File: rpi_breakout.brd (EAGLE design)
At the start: 33 x 54 mm, 21 parts

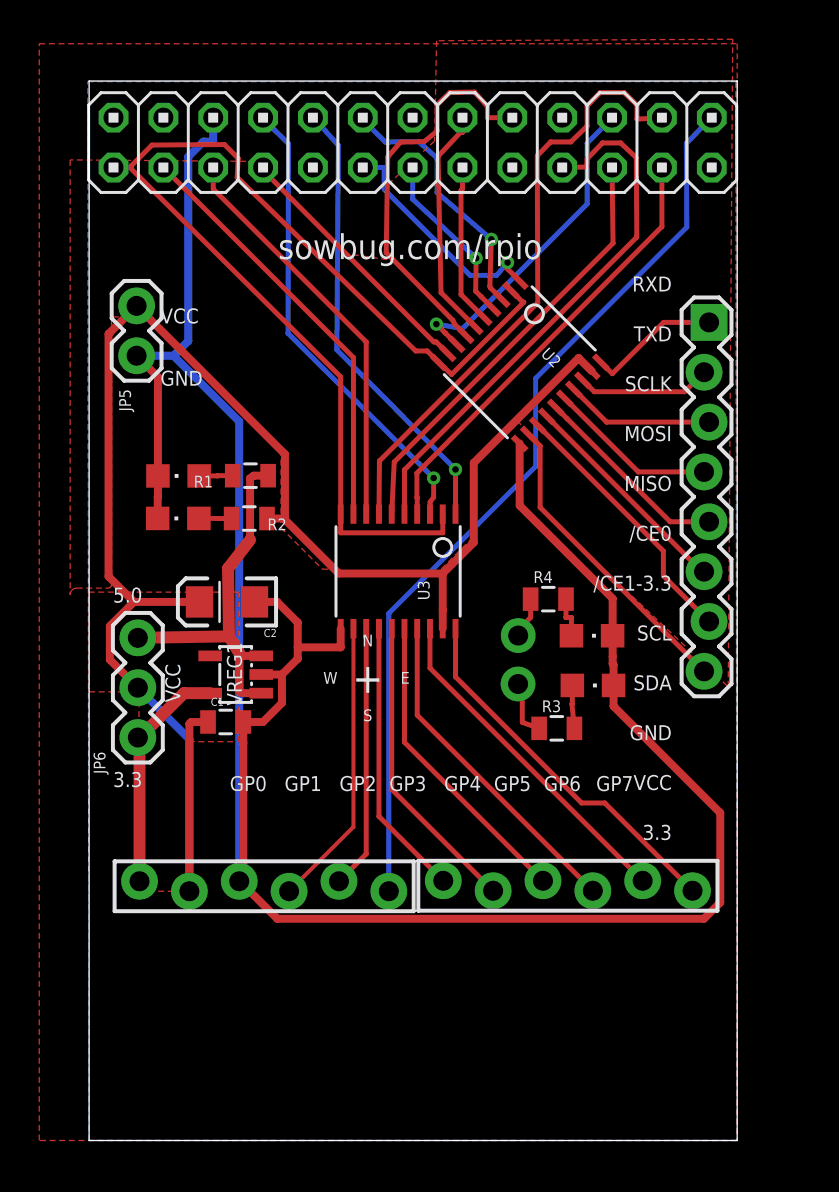
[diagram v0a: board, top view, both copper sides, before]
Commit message: Much nicer routing, with the help of peterobinson
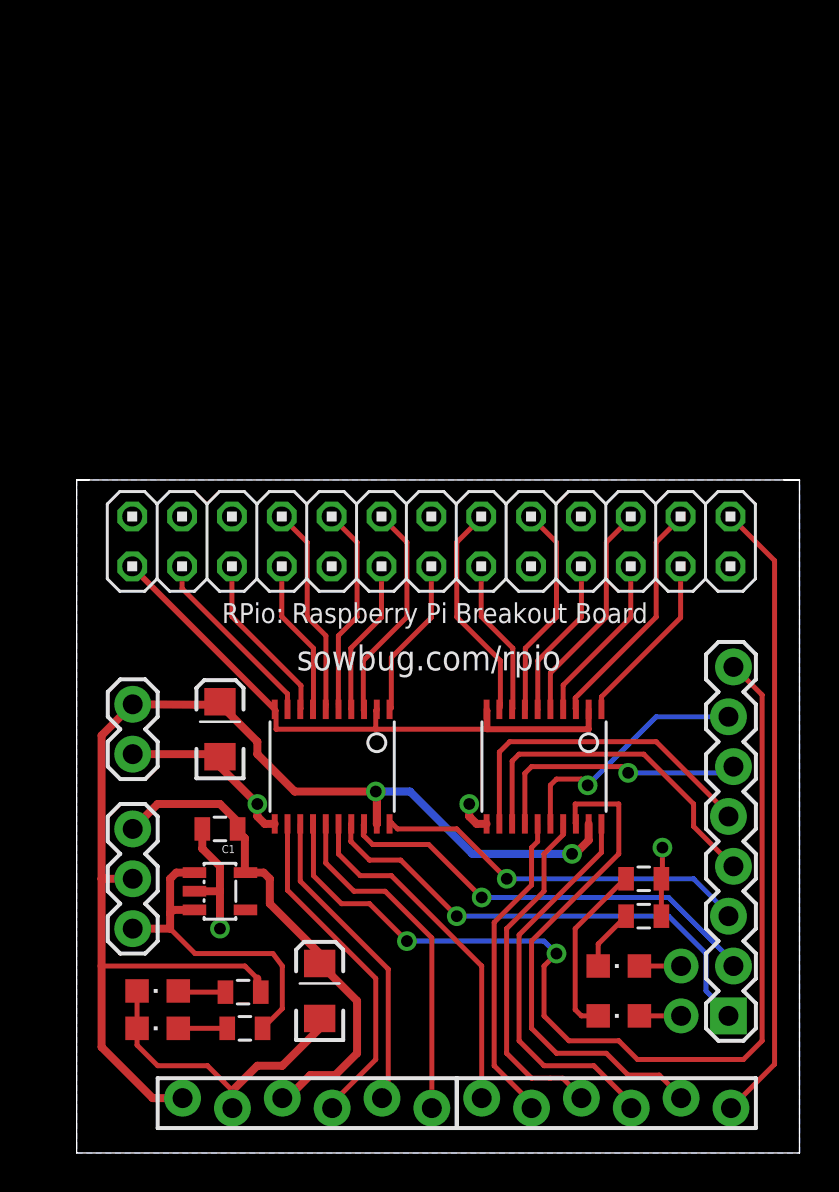
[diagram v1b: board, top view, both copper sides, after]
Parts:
- added C3: 10uF, SparkFun:EIA3216
- JP2: device SparkFun:1X08_LOCK -> rpi_breakout:1X08_LOCK
- U2, U3: device adafruit:TSSOP20 -> rpi_breakout:TSSOP20
- moved JP2 35.4 mm to (32.7, 6.35), turned to 90 degrees
- moved LED1 28.2 mm to (3.49, 5.71)
- moved R1 28.2 mm to (7.94, 5.71)
- moved R2 24.1 mm to (7.85, 7.56)
- moved LED2 24.1 mm to (3.49, 7.62)
- moved JP8 21.1 mm to (30.2, 6.35)
- moved U2 20.6 mm to (23.2, 19.1), turned to 180 degrees
- moved C2 20.4 mm to (11.7, 7.62), turned to 90 degrees
- moved JP1 20.3 mm to (17.4, 30.5)
- moved JP5 20.3 mm to (2.22, 22.2)
- moved LED4 19.4 mm to (27.0, 6.35), turned to 90 degrees
- moved JP7 16.6 mm to (30.2, 8.89)
- moved R4 15.1 mm to (28.3, 13.3)
- moved LED3 14.4 mm to (27.0, 8.89), turned to 90 degrees
- moved JP3 11.3 mm to (4.76, 1.91)
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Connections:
- removed net LED3_A: LED3.A, R3.2
- removed net LED4_A: LED4.A, R4.2
- new net N$3: LED3.C, R3.1
- new net N$4: LED4.C, R4.1
- net /SPI_CE0: now also U2.3; no longer U3.7
- net /SPI_CE1: now also JP4.6; no longer JP3.6
- net /SPI_CEV0: now also JP4.5, U2.18; no longer JP4.1, U3.14
- net 3.3V: now also C1.1, C2.A, JP3.3; no longer JP3.1
- net GND: now also C3.C, JP3.2, R3.2, R4.2; no longer JP3.3, LED3.C, LED4.C
- net GPIOV_0: now also U3.17; no longer U2.20
- net GPIOV_1: now also U3.18; no longer U2.18
- net GPIOV_2: now also U3.20; no longer U2.17
- net GPIOV_3: now also U2.13; no longer U2.16
- net GPIOV_4: now also U2.12; no longer U2.15
- net GPIOV_6: now also U2.16; no longer U2.13
- net GPIOV_7: now also U3.14; no longer U2.12
- net GPIO_0: now also U3.4; no longer U2.1
- net GPIO_1: now also U3.3; no longer U2.3
- net GPIO_2: now also U3.1; no longer U2.4
- net GPIO_3: now also U2.8; no longer U2.5
- net GPIO_4: now also U2.9; no longer U2.6
- net GPIO_6: now also U2.5; no longer U2.8
- net GPIO_7: now also U3.7; no longer U2.9
- net LED3_JP: now also LED3.A; no longer R3.1
- net LED4_JP: now also LED4.A; no longer R4.1
- net RXD: now also U3.5; no longer U3.1
- net RXDV: now also JP4.1, U3.16; no longer JP4.6, U3.20
- net SPI_MISO: now also U2.4; no longer U3.6
- net SPI_MISOV: now also JP4.3, U2.17; no longer JP4.2, U3.15
- net SPI_MOSI: now also U2.6; no longer U3.5
- net SPI_MOSIV: now also JP4.2, U2.15; no longer JP4.3, U3.16
- net SPI_SCLK: now also U2.1; no longer U3.4
- net SPI_SCLKV: now also U2.20; no longer U3.17
- net TXD: now also U3.6; no longer U3.3
- net TXDV: now also JP3.6, U3.15; no longer JP4.5, U3.18
- net VCC: now also C3.A, JP3.1; no longer C1.1, C2.A, JP3.2
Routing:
- net GND: track 127.2 -> 37.1 mm, vias 0 -> 4
- net GPIOV_7: track 15.8 -> 52.3 mm, vias 0 -> 2
- net 3V3_RPI: track 58.6 -> 31.4 mm
- net VCC: track 87.7 -> 65.3 mm, vias 0 -> 2
- net SPI_MOSI: track 27.9 -> 8.29 mm
- net /SPI_CE0: track 30.9 -> 12.1 mm
- net GPIOV_0: track 6.84 -> 25.4 mm, vias 0 -> 1
- net GPIOV_1: track 6.83 -> 22.3 mm, vias 0 -> 1
- net /SPI_CE1: track 46.6 -> 32.0 mm
- net 3.3V: track 11.9 -> 26.1 mm
- net SPI_SCLK: track 22.8 -> 8.96 mm
- net SPI_MISO: track 22.3 -> 8.71 mm
- net TXD: track 23.9 -> 10.9 mm, vias 1 -> 0
- net RXD: track 23.5 -> 10.9 mm, vias 1 -> 0
- net SDA0: track 21.7 -> 9.51 mm
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- added copper zone on layer 16, net GND
- removed copper zone on layer 1, net GND
- removed copper zone on layer 16, net N$3
- removed copper zone on layer 1, net VCC
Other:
- board size 33 x 54 mm -> 36.8 x 34.3 mm
- board text removed: "+"
- board text removed: "/CE0"
- board text removed: "/CE1-3.3"
- board text removed: "3.3"
- board text removed: "5.0"
- board text removed: "DANGER: CE1 is always 3.3V!"
- board text removed: "E"
- board text removed: "GND"
- board text removed: "GP0"
- board text removed: "GP1"
- board text removed: "GP2"
- board text removed: "GP3"
- board text removed: "GP4"
- board text removed: "GP5"
- board text removed: "GP6"
- board text removed: "GP7"
- board text removed: "MISO"
- board text removed: "MOSI"
- board text removed: "N"
- board text removed: "RXD"
- board text removed: "S"
- board text removed: "SCL"
- board text removed: "SCLK"
- board text removed: "SDA"
- board text removed: "TXD"
- board text removed: "VCC"
- board text removed: "W"
- board text removed: "sowbug.com"
- board text removed: "v0.0.2"
